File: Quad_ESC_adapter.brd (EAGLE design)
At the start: 101.6 x 41.1 mm, 13 parts, among them J1 IBPD-SOCKET, J2 IBPD-SOCKET, J3 IBPD-SOCKET, J4 IBPD-SOCKET

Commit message: Example placement for adapter
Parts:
- moved C6 151.9 mm to (61.0, 7.62), flipped to the bottom, turned to 90 degrees
- moved C5 126.7 mm to (49.5, 7.62), flipped to the bottom, turned to 90 degrees
- moved J2 104.9 mm to (10.2, 10.2), turned to 90 degrees
- moved C1 99.1 mm to (38.1, 7.62), flipped to the bottom, turned to 90 degrees
- moved J1 28.2 mm to (10.2, 29.2), turned to 90 degrees

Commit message: moved stuff around
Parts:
- moved J4 149.1 mm to (91.4, 6.99), turned to 270 degrees
- moved H4 147.2 mm to (98.3, 17.4)
- moved H3 130.1 mm to (98.4, 38.0)
- moved J3 125.6 mm to (91.4, 27.7), turned to 270 degrees
- moved H2 119.3 mm to (3.30, 17.2)
- moved H1 102.5 mm to (3.30, 37.8)
- moved J2 3.30 mm to (10.2, 6.86)
- moved J1 1.70 mm to (10.3, 27.5)

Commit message: moved stuff around
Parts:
- moved C1 9.40 mm to (39.4, 16.9)
- moved C5 9.40 mm to (50.8, 16.9)
- moved C6 9.40 mm to (62.3, 16.9)
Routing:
- added copper zone on layer 1, net 12V
- added copper zone on layer 1, net ESC3_B
- added copper zone on layer 1, net ESC3_R
- added copper zone on layer 1, net ESC3_Y
- added copper zone on layer 1, net GND
- added copper zone on layer 16, net GND

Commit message: Finalized as best I could
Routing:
- added copper zone on layer 16, net 12V
- added copper zone on layer 1, net ESC1_B
- added copper zone on layer 1, net ESC1_R
- added copper zone on layer 1, net ESC1_Y
- added copper zone on layer 1, net ESC2_B
- added copper zone on layer 1, net ESC2_R
- added copper zone on layer 1, net ESC2_Y
- added copper zone on layer 1, net ESC4_B
- added copper zone on layer 1, net ESC4_R
- added copper zone on layer 1, net ESC4_Y

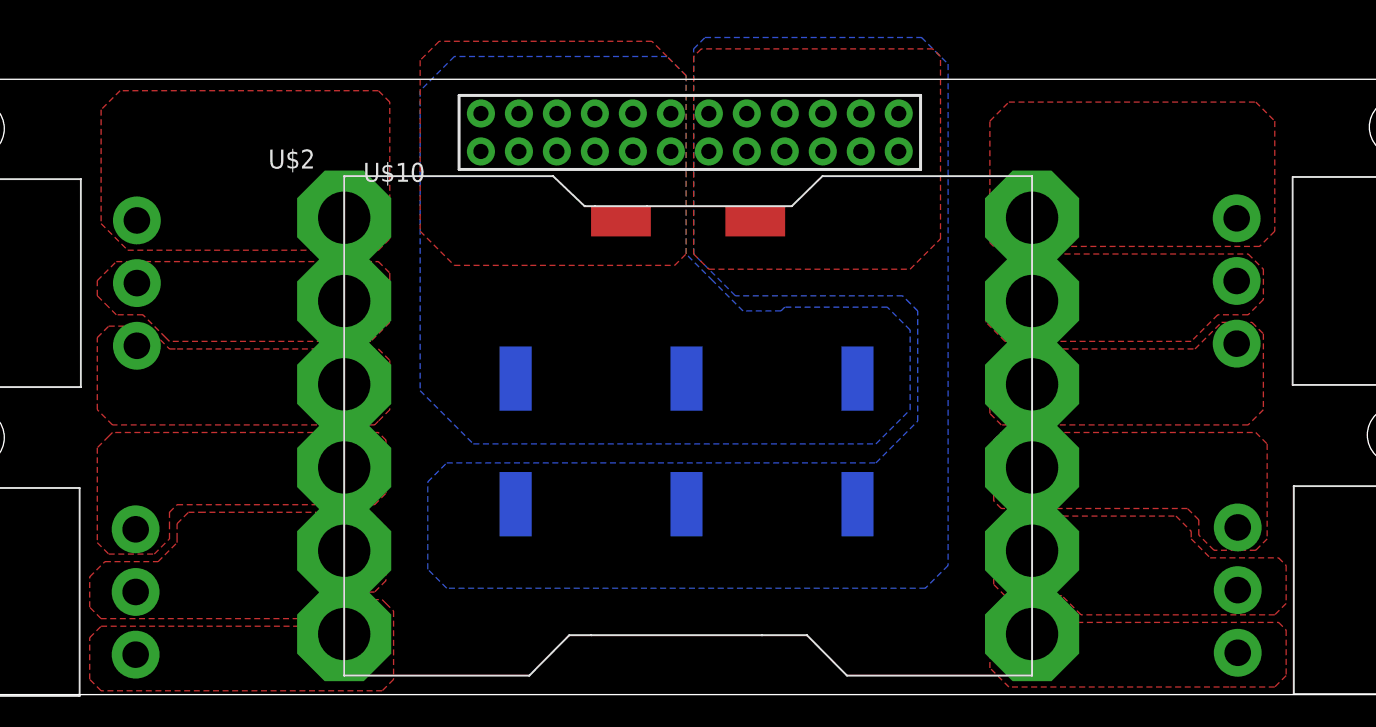
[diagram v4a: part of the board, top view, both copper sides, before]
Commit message: thicc copper
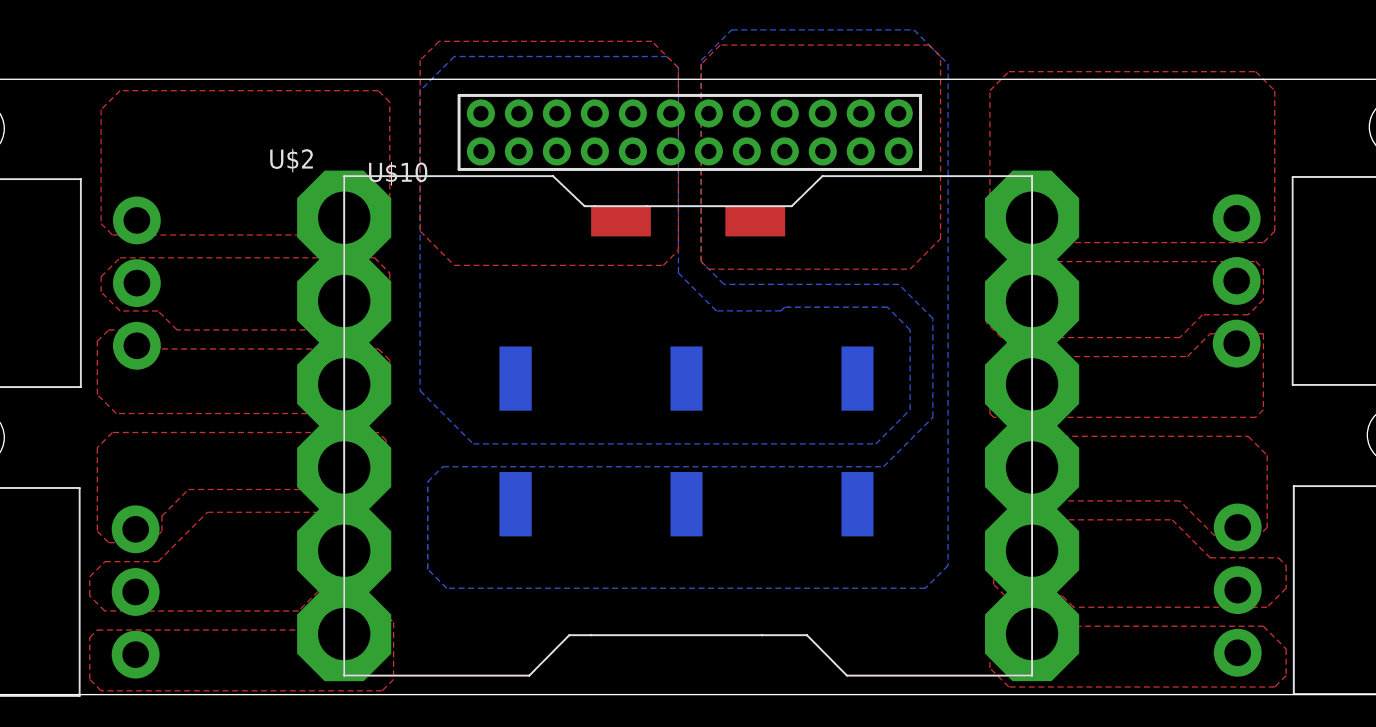
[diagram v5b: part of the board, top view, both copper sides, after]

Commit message: done bish
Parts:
- removed U$10: LUMENIER_QUAD-NO-CUT, Lumenier ESC:LUMENIER_QUAD-NO-CUT
- added U$1: LUMENIER_QUAD, AUX, Lumenier ESC:LUMENIER_QUAD
- moved C1 19.9 mm to (56.6, 6.94), turned to 270 degrees
- moved C6 19.8 mm to (45.8, 28.0), turned to 0 degrees
- moved C5 11.5 mm to (45.2, 6.94), turned to 270 degrees
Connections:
- net 12V: now also U$1.VIN; no longer U$10.VIN
- net ESC1_B: now also U$1.1; no longer U$10.1
- net ESC1_R: now also U$1.3; no longer U$10.3
- net ESC1_Y: now also U$1.2; no longer U$10.2
- net ESC2_B: now also U$1.4; no longer U$10.4
- net ESC2_R: now also U$1.6; no longer U$10.6
- net ESC2_Y: now also U$1.5; no longer U$10.5
- net ESC3_B: now also U$1.12; no longer U$10.12
- net ESC3_R: now also U$1.10; no longer U$10.10
- net ESC3_Y: now also U$1.11; no longer U$10.11
- net ESC4_B: now also U$1.9; no longer U$10.9
- net ESC4_R: now also U$1.7; no longer U$10.7
- net ESC4_Y: now also U$1.8; no longer U$10.8
- net GND: now also U$1.GND; no longer U$10.GND
